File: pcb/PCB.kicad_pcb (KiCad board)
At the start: 4 copper layers, 29.2 x 51.1 mm, 35 parts, among them J1 Conn_01x15, J2 USB_C_Receptacle_USB2.0, J3 Conn_01x15, J4 TC2030, J5 Conn_01x04, SW1 SW_Push, SW2 SW_Push, U1 SN65HVD230, U2 AMS1117-3.3, U3 STM32F103C8T6, Y1 8MHz

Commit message: pcb update precharge
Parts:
- removed C10, C12, C6, C8, C9: 100n, Capacitor_SMD:C_0402_1005Metric
- removed C11, C2, C3: 1u, Capacitor_SMD:C_0603_1608Metric
- removed C4: 4u7, Capacitor_SMD:C_0603_1608Metric
- removed C5, C7: 30p, Capacitor_SMD:C_0402_1005Metric
- removed FB1, FB2: 100R@100MHz, Resistor_SMD:R_0805_2012Metric
- removed J4: TC2030, Connector:Tag-Connect_TC2030-IDC-NL_2x03_P1.27mm_Vertical
- removed J5: Conn_01x04, Connector_PinHeader_2.54mm:PinHeader_1x04_P2.54mm_Vertical
- removed JP1: SolderJumper_Bridged, Jumper:SolderJumper-2_P1.3mm_Bridged_RoundedPad1.0x1.5mm
- removed SW1, SW2: SW_Push, Button_Switch_SMD:SW_Push_1P1T_NO_CK_KSC7xxJ
- removed Y1: 8MHz, Crystal:Crystal_SMD_5032-2Pin_5.0x3.2mm
- added K1: AZDC6, AZDC6:AZDC6, F.Cu at (64.8, 114.9)
- added K2: dbt71205u21, dbt71205u:DBT71205U, F.Cu at (89.5, 106.6)
- added Q1: IRLZ44N, Package_TO_SOT_SMD:TO-263-3_TabPin2, F.Cu at (61.0, 85.4)
- added R10: 1k, Resistor_SMD:R_0603_1608Metric, F.Cu at (58.5, 97.3)
- added R11: 10K, Resistor_SMD:R_0603_1608Metric, F.Cu at (63.6, 97.3)
- added R8: hsa255k6j, hsa255k6j:hsa255k6j, F.Cu at (150.5, 113.8)
- added R9: 680, Resistor_SMD:R_0603_1608Metric, F.Cu at (78.1, 108.7)
- C1: footprint Capacitor_SMD:C_0402_1005Metric -> Capacitor_SMD:C_0603_1608Metric
- D1: value YELLOW -> SMAJ15CA; footprint LED_SMD:LED_0603_1608Metric -> Diode_SMD:D_SMA
- D2: value BLUE -> SMAJ15CA; footprint LED_SMD:LED_0603_1608Metric -> Diode_SMD:D_SMA
- J1: value Conn_01x15 -> TE 770966-2; footprint Connector_PinHeader_2.54mm:PinHeader_1x15_P2.54mm_Vertical -> Connector_TE-Connectivity:TE_MATE-N-LOK_1-770966-x_1x02_P4.14mm_Horizontal
- J2: value USB_C_Receptacle_USB2.0 -> TE 770966-2; footprint Connector_USB:USB_C_Receptacle_HRO_TYPE-C-31-M-12 -> Connector_TE-Connectivity:TE_MATE-N-LOK_1-770966-x_1x02_P4.14mm_Horizontal
- J3: value Conn_01x15 -> JST B04B-XASK; footprint Connector_PinHeader_2.54mm:PinHeader_1x15_P2.54mm_Vertical -> Connector_JST:JST_XA_B04B-XASK-1_1x04_P2.50mm_Vertical
- R1: value 5k1 -> hsa255k6j; footprint Resistor_SMD:R_0402_1005Metric -> hsa255k6j:hsa255k6j
- R2, R5: value 5k1 -> 5M; footprint Resistor_SMD:R_0402_1005Metric -> Resistor_SMD:R_1206_3216Metric
- R3: value 120R -> 5M; footprint Resistor_SMD:R_0402_1005Metric -> Resistor_SMD:R_1206_3216Metric
- R4: value 1k5 -> 110k; footprint Resistor_SMD:R_0402_1005Metric -> Resistor_SMD:R_1206_3216Metric
- R6: value 1k5 -> 5M; footprint Resistor_SMD:R_0402_1005Metric -> Resistor_SMD:R_1206_3216Metric
- R7: value 1k5 -> 100k; footprint Resistor_SMD:R_0402_1005Metric -> Resistor_SMD:R_1206_3216Metric
- U1: value SN65HVD230 -> LM339; footprint Package_SO:SOIC-8_3.9x4.9mm_P1.27mm -> Package_SO:TSSOP-14_4.4x5mm_P0.65mm
- U2: value AMS1117-3.3 -> LTV-817S; footprint Package_TO_SOT_SMD:SOT-223-3_TabPin2 -> Package_DIP:SMDIP-4_W9.53mm
- U3: value STM32F103C8T6 -> VRB1205YMD-15WR3; footprint Package_QFP:LQFP-48_7x7mm_P0.5mm -> VRB1205YMD-6WR3:VRB1205YMD-15WR3
- moved J3 99.7 mm to (60.3, 111.2), turned to 90 degrees
- moved U3 91.2 mm to (66.7, 63.0), turned to 0 degrees
- moved R7 78.9 mm to (103.7, 51.5), turned to 180 degrees
- moved D1 78.7 mm to (103.8, 64.5), turned to 0 degrees
- moved D2 75.1 mm to (103.5, 59.1), turned to 0 degrees
- moved U2 71.1 mm to (73.0, 103.6), turned to 180 degrees
- moved R4 61.1 mm to (116.0, 74.0), turned to 180 degrees
- moved C1 56.5 mm to (103.5, 79.5), turned to 90 degrees
- moved U1 55.3 mm to (108.6, 79.5), turned to 90 degrees
- moved R1 54.8 mm to (150.5, 142.9), turned to 180 degrees
- moved R3 50.8 mm to (124.1, 77.9), turned to 180 degrees
- moved R6 40.8 mm to (125.1, 54.1), turned to 180 degrees
- moved R5 39.0 mm to (132.7, 54.1), turned to 180 degrees
- moved J1 34.4 mm to (138.1, 54.5)
- moved R2 18.0 mm to (131.8, 77.9), turned to 180 degrees
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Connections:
- C1 pad 1: +3V3 -> +5V
- C1 pad 2: GND -> TS-
- D1 pad 1: Net-(D1-Pad1) -> TS-
- D1 pad 2: +3V3 -> Net-(D1-Pad2)
- D2 pad 1: Net-(D2-Pad1) -> TS-
- D2 pad 2: /LED_STAT -> Net-(D2-Pad2)
- J1 pad 1: +3V3 -> TS+
- J1 pad 2: GND -> TS-
- J3 pad 1: +3V3 -> +12V
- J3 pad 3: PA10 -> Net-(J3-Pad3)
- J3 pad 4: PA9 -> unconnected-(J3-Pad4)
- R1 pad 1: Net-(J2-PadA5) -> TS+
- R1 pad 2: GND -> Net-(K1-Pad1)
- R2 pad 1: GND -> Precharge
- R2 pad 2: Net-(J2-PadB5) -> Net-(R2-Pad2)
- R3 pad 1: /CAN+ -> Net-(R2-Pad2)
- R3 pad 2: Net-(JP1-Pad2) -> Net-(D1-Pad2)
- R4 pad 1: Net-(D1-Pad1) -> Net-(D1-Pad2)
- R4 pad 2: GND -> TS-
- R5 pad 1: /BOOT0 -> TS+
- R5 pad 2: GND -> Net-(R5-Pad2)
- R6 pad 1: +3V3 -> Net-(R5-Pad2)
- R6 pad 2: USB_D+ -> Net-(D2-Pad2)
- R7 pad 1: Net-(D2-Pad1) -> Net-(D2-Pad2)
- R7 pad 2: GND -> TS-
- U1 pad 1: CANTX -> (no net)
- U1 pad 2: GND -> Net-(U1-Pad2)
- U1 pad 3: +3V3 -> +5V
- U1 pad 4: CANRX -> Net-(D2-Pad2)
- U1 pad 5: unconnected-(U1-Pad5) -> Net-(D1-Pad2)
- U1 pad 6: /CAN- -> (no net)
- U1 pad 7: /CAN+ -> (no net)
- U1 pad 8: GND -> (no net)
- U2 pad 1: GND -> Net-(R9-Pad2)
- U2 pad 2: +3V3 -> Net-(U1-Pad2)
- U2 pad 3: VCC -> Net-(R10-Pad2)
- U3 pad 1: +3V3 -> +12V
- U3 pad 2: PC13 -> GND
- U3 pad 3: PC14 -> +12V
- U3 pad 4: PC15 -> +5V
- U3 pad 5: /HSE_OUT -> unconnected-(U3-Pad5)
- U3 pad 6: /HSE_IN -> TS-
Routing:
- net TS-: track 0.00 -> 116.4 mm, vias 0 -> 2
- net TS+: track 0.00 -> 98.9 mm
- net Precharge: track 0.00 -> 87.6 mm
- net Net-(D2-Pad2): track 0.00 -> 58.2 mm
- net Discharge: track 0.00 -> 55.8 mm
- net +3V3: track 44.0 -> 0.00 mm, vias 18 -> 0
- net Net-(U1-Pad2): track 0.00 -> 40.3 mm
- net /NRST: track 35.9 -> 0.00 mm, vias 3 -> 0
- net /BOOT0: track 31.5 -> 0.00 mm, vias 3 -> 0
- net +12V: track 0.00 -> 26.8 mm, vias 0 -> 1
- net SWDIO: track 24.1 -> 0.00 mm, vias 2 -> 0
- net Net-(D1-Pad2): track 0.00 -> 23.8 mm
- net SWO: track 22.9 -> 0.00 mm, vias 2 -> 0
- net Net-(K1-Pad1): track 0.00 -> 22.4 mm
- net USB_D-: track 21.7 -> 0.00 mm
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- added copper zone on In2.Cu, net +12V
- added copper zone on In1.Cu, net TS-
- removed copper zone on In2.Cu, net +3V3
- removed copper zone on B.Cu, net GND
- removed copper zone on F.Cu, net unconnected-(J2-PadS1)
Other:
- board size 29.2 x 51.1 mm -> 100 x 100 mm
- board text removed: "3V3"
- board text removed: "3V3 +CAN- GND"
- board text removed: "A0"
- board text removed: "A10"
- board text removed: "A13"
- board text removed: "A14"
- board text removed: "A15"
- board text removed: "A2"
- board text removed: "A3"
- board text removed: "A4"
- board text removed: "A5"
- board text removed: "A6"
- board text removed: "A7"
- board text removed: "A8"
- board text removed: "A9"
- board text removed: "B0"
- board text removed: "B1"
- board text removed: "B10"
- board text removed: "B11"
- board text removed: "B2"
- board text removed: "B3"
- board text removed: "B4"
- board text removed: "B5"
- board text removed: "B6"
- board text removed: "B7"
- board text removed: "BOOT"
- board text removed: "C13"
- board text removed: "C14"
- board text removed: "C15"
- board text removed: "CAN TERM"
- board text removed: "GND"
- board text removed: "GND -CAN+ 3V3"
- board text removed: "JLCJLCJLCJLC"
- board text removed: "RESET"
- board text removed: "Rev 1"
- board text removed: "STM32F103 CAN/USB-C Jack LeFevre July 2022"
- board text removed: "SWCLK"
- board text removed: "SWDIO"
- board text removed: "SWO"

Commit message: bbs home
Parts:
- moved C1 3.74 mm to (107.2, 79.4)
- moved U3 2.93 mm to (67.0, 60.0)
- moved U1 2.46 mm to (111.0, 79.5)
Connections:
- net Net-(J3-Pad3) renamed /AIR
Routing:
- net +5V: track 5.92 -> 90.6 mm
- net /AIR: track 0.00 -> 37.3 mm
- net TS-: track 116.4 -> 95.6 mm
- net Net-(D1-Pad2): track 23.8 -> 41.3 mm, vias 0 -> 2
- net Net-(K2-Pad1): track 15.1 -> 17.8 mm
- net Precharge: track 87.6 -> 89.9 mm
- net Net-(D2-Pad2): track 58.2 -> 60.0 mm
- net +12V: track 26.8 -> 28.5 mm
- net TS+: track 98.9 -> 97.3 mm
- net Net-(U1-Pad2): track 40.3 -> 41.3 mm
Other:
- board text added: "+12V"
- board text added: "AIR"
- board text added: "Bronco Racing Rev 1 Pre/Discharge Circuit Alexander Adams, 2023"
- board text added: "Discharge"
- board text added: "GLV :^)"
- board text added: "GND"
- board text added: "High Voltage"
- board text added: "Precharge"
- board text added: "TS+"
- board text added: "TS-"

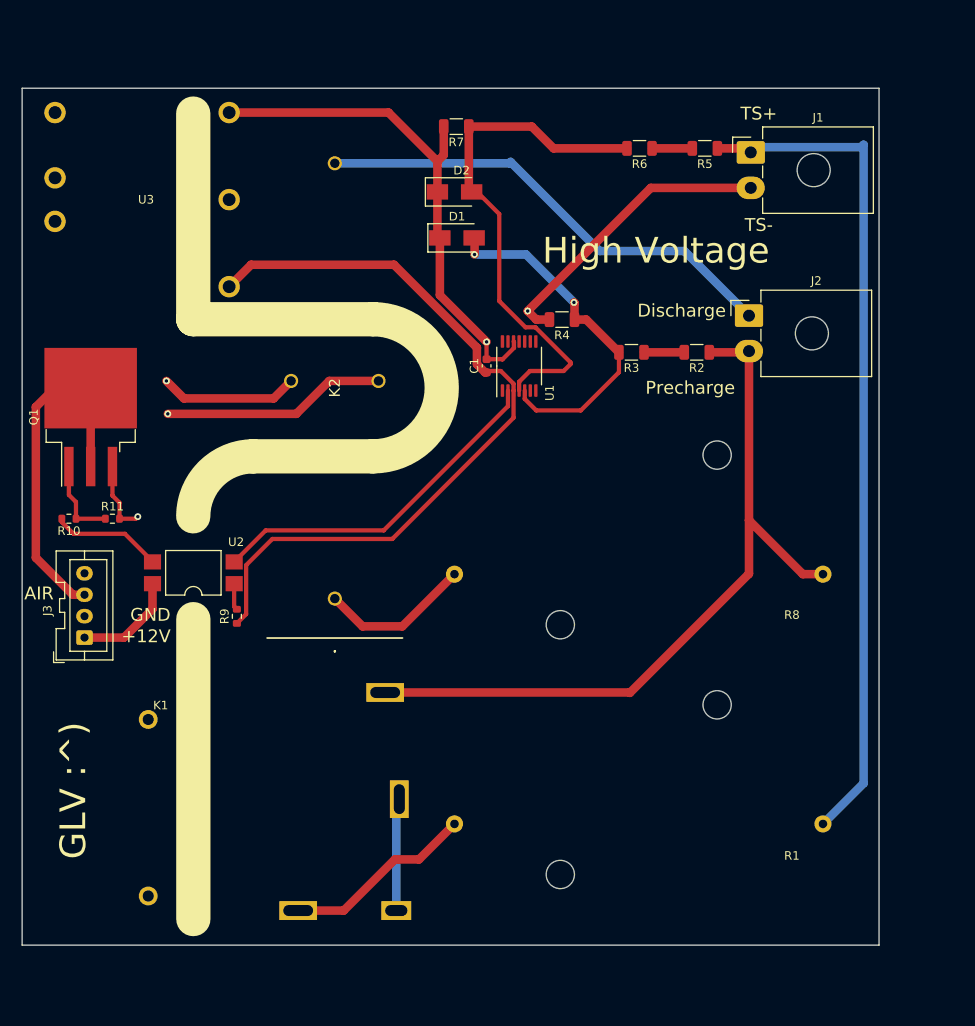
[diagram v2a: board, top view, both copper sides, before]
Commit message: Added mounting holes and fixed drc violations
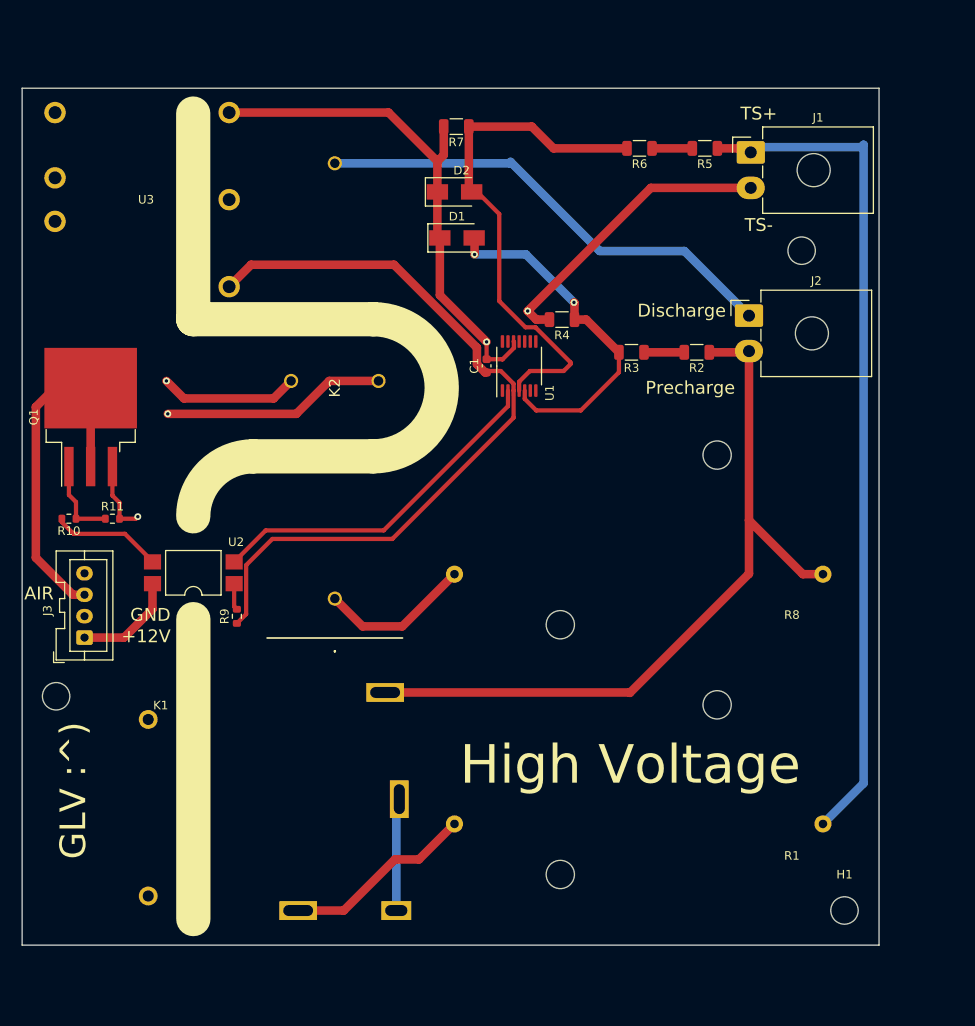
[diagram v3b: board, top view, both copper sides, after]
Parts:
- added H1: MountingHole, MountingHole:MountingHole_3.2mm_M3, F.Cu at (149.0, 143.0)
- added H2: MountingHole, MountingHole:MountingHole_3.2mm_M3, F.Cu at (144.0, 66.0)
- added H3: MountingHole, MountingHole:MountingHole_3.2mm_M3, F.Cu at (57.0, 118.0)

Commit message: Final? Pre/Dis
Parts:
- added C2: 100u, Capacitor_SMD:CP_Elec_6.3x7.7, F.Cu at (104.5, 71.0)
- added C3: 100u, Capacitor_SMD:CP_Elec_6.3x7.7, F.Cu at (75.5, 82.5)
- added D3: SMAJ15CA, Diode_SMD:D_SMA, F.Cu at (67.5, 94.0)
- added D4: ssb43L, Diode_SMD:D_SMB, F.Cu at (60.0, 97.0)
- added G***: LOGO, PLZ WORK:EEEELLLLLZZZ, B.Cu at (127.5, 100.0)
- added G***: LOGO, PLZ WORK:Bold, B.Cu at (62.3, 72.4)
- added R12: 24R, Resistor_SMD:R_2512_6332Metric, F.Cu at (60.0, 126.5)
- moved R11 6.36 mm to (62.6, 91.0)
- moved R10 6.36 mm to (57.5, 91.0)
- moved Q1 4.04 mm to (61.0, 81.4)
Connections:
- K1 pad 5: +12V -> Net-(K1-Pad5)
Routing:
- net Net-(K1-Pad5): track 0.00 -> 14.1 mm
- net +12V: track 28.5 -> 36.7 mm, vias 1 -> 4
- net /AIR: track 37.3 -> 44.7 mm
- net Net-(R10-Pad2): track 12.9 -> 19.8 mm
- net Net-(Q1-Pad1): track 9.86 -> 7.34 mm
- net +5V: track 90.6 -> 91.8 mm
- net GND: track 34.8 -> 35.7 mm, vias 2 -> 3
- net Net-(D2-Pad2): track 60.0 -> 60.6 mm

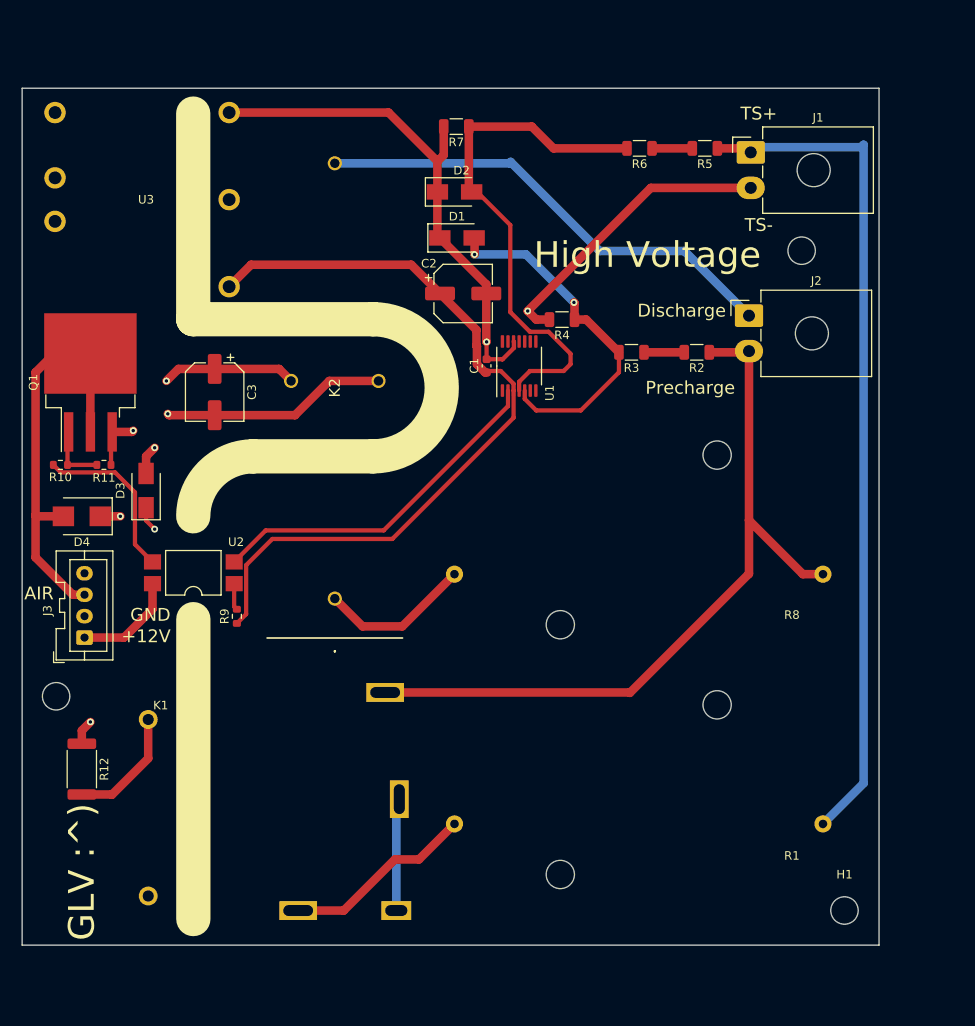
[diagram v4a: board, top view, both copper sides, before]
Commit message: Re-layout pcb for br24
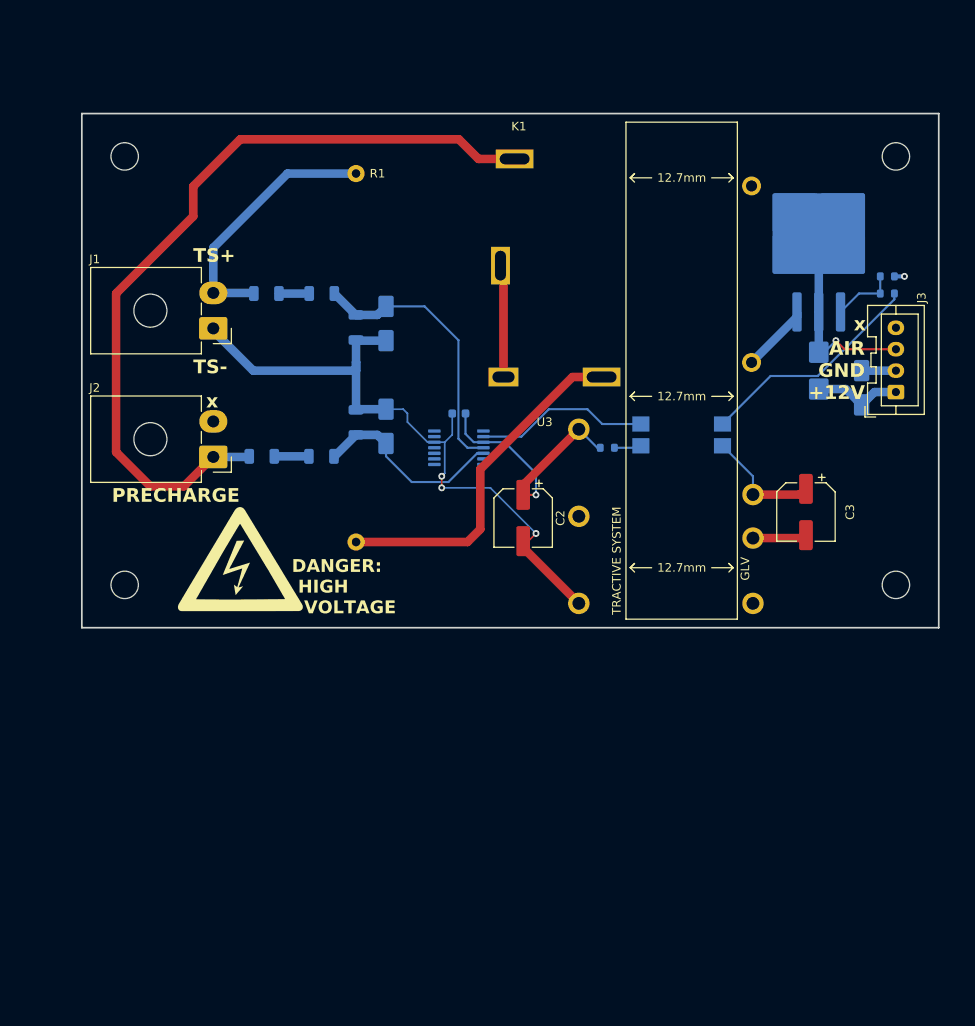
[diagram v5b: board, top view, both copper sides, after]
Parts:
- removed K2: dbt71205u21, dbt71205u:DBT71205U
- removed R12: 24R, Resistor_SMD:R_2512_6332Metric
- removed R8: hsa255k6j, hsa255k6j:hsa255k6j
- added G***: LOGO, PLZ WORK:voltage, F.Cu at (78.5, 102.0)
- added G***: LOGO, PLZ WORK:voltage, B.Cu at (97.0, 102.0)
- added H4: MountingHole, MountingHole:MountingHole_3.2mm_M3, F.Cu at (65.0, 105.0)
- C1, D1, D2, D3, D4, Q1, R10, R11, R2, R3, R4, R5, R6, R7, R9, U1, U2: moved to B.Cu
- moved R1 100.3 mm to (106.0, 53.0), turned to -90 degrees
- moved J3 98.9 mm to (155.0, 82.5)
- moved R10 98.6 mm to (154.0, 71.0), turned to 0 degrees
- moved K1 98.4 mm to (141.1, 52.6)
- moved R11 94.0 mm to (154.0, 69.0)
- moved G*** 88.3 mm to (146.0, 100.5)
- moved H1 88.2 mm to (155.0, 55.0)
- moved D4 87.7 mm to (146.0, 80.0), turned to 90 degrees
- moved Q1 86.5 mm to (146.0, 65.5)
- moved D3 84.4 mm to (151.0, 82.0), turned to -90 degrees
- moved U3 71.4 mm to (128.2, 97.0), turned to 180 degrees
- moved C3 70.4 mm to (144.5, 96.5)
- moved J1 66.0 mm to (75.3, 75.1), turned to 180 degrees
- moved J2 64.7 mm to (75.3, 90.1), turned to 180 degrees
- moved H3 63.5 mm to (65.0, 55.0)
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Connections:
- J1 pad 1: TS+ -> TS-
- J1 pad 2: TS- -> TS+
- J2 pad 1: Discharge -> Precharge
- J2 pad 2: Precharge -> unconnected-(J2-Pin_2-Pad2)
- K1 pad 5: Net-(K1-Pad5) -> +12V
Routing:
- net TS+: track 97.3 -> 30.3 mm
- net +5V: track 91.8 -> 30.3 mm, vias 0 -> 1
- net Discharge: track 55.8 -> 0.00 mm
- net Net-(D2-A2): track 60.6 -> 32.4 mm
- net Net-(U1-Pad2): track 41.3 -> 20.4 mm
- net /AIR: track 44.7 -> 23.8 mm, vias 0 -> 1
- net Net-(K1-Pad1): track 22.4 -> 40.7 mm
- net Net-(D1-A2): track 41.3 -> 23.0 mm, vias 2 -> 0
- net Net-(K2-Pad1): track 17.8 -> 0.00 mm
- net TS-: track 95.6 -> 78.3 mm, vias 2 -> 3
- net GND: track 35.7 -> 19.6 mm, vias 3 -> 1
- net Net-(K1-Pad5): track 14.1 -> 0.00 mm
- net +12V: track 36.7 -> 24.0 mm, vias 4 -> 0
- net Net-(R10-Pad2): track 19.8 -> 26.8 mm
- net Precharge: track 89.9 -> 94.1 mm
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- removed copper zone on In1.Cu, net TS-
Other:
- board size 100 x 100 mm -> 100 x 60 mm
- board text added: "12.7mm"
- board text added: "AIR G +V"
- board text added: "AIR GND +12V"
- board text added: "Alexander Adams, Josh Iwick, & Jack LeFevre Jan 2024"
- board text added: "Bronco Racing Rev 2 Precharge Circuit"
- board text added: "DANGER: HIGH VOLTAGE"
- board text added: "GLV"
- board text added: "PRECHARGE"
- board text added: "TRACTIVE SYSTEM"
- board text added: "x"
- board text removed: "+12V"
- board text removed: "AIR"
- board text removed: "Bronco Racing Rev 1 Pre/Discharge Circuit Alexander Adams, 2023"
- board text removed: "Discharge"
- board text removed: "GLV :^)"
- board text removed: "GND"
- board text removed: "High Voltage"
- board text removed: "Precharge"
